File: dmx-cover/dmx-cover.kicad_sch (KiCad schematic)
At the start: 7 parts

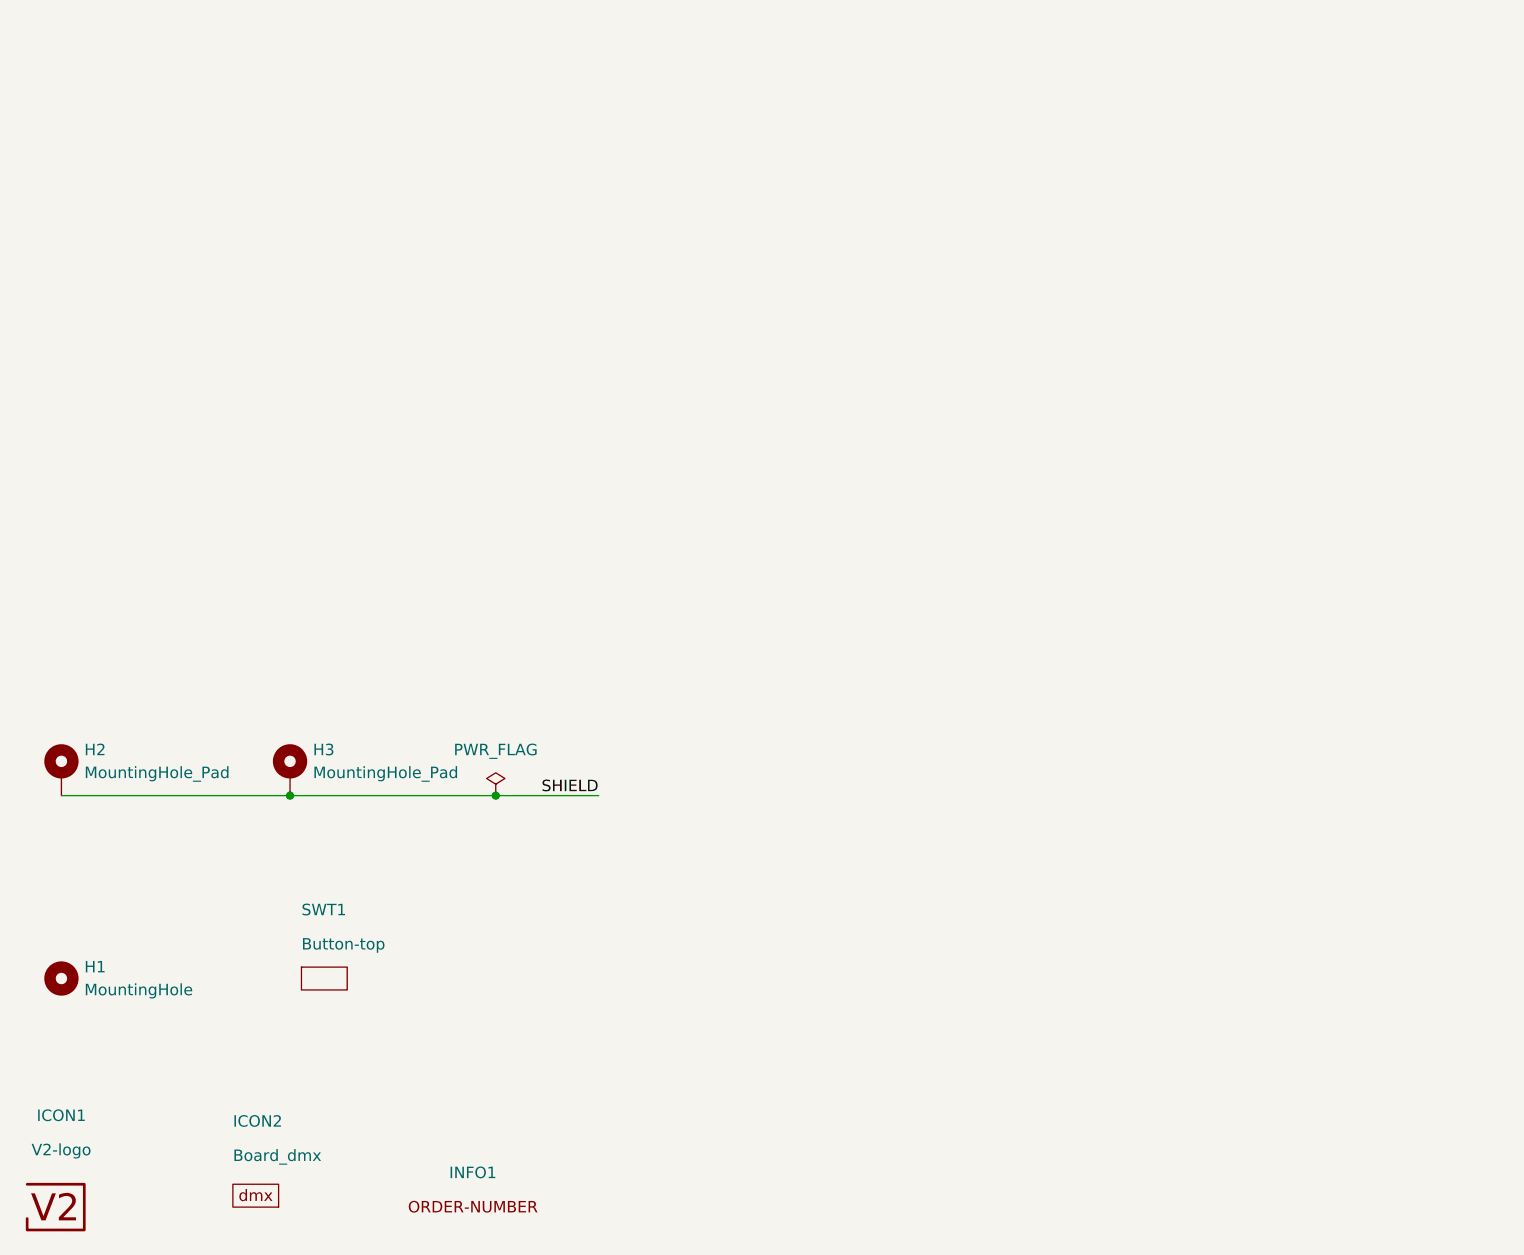
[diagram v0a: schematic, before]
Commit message: Update to KiCad 7.0
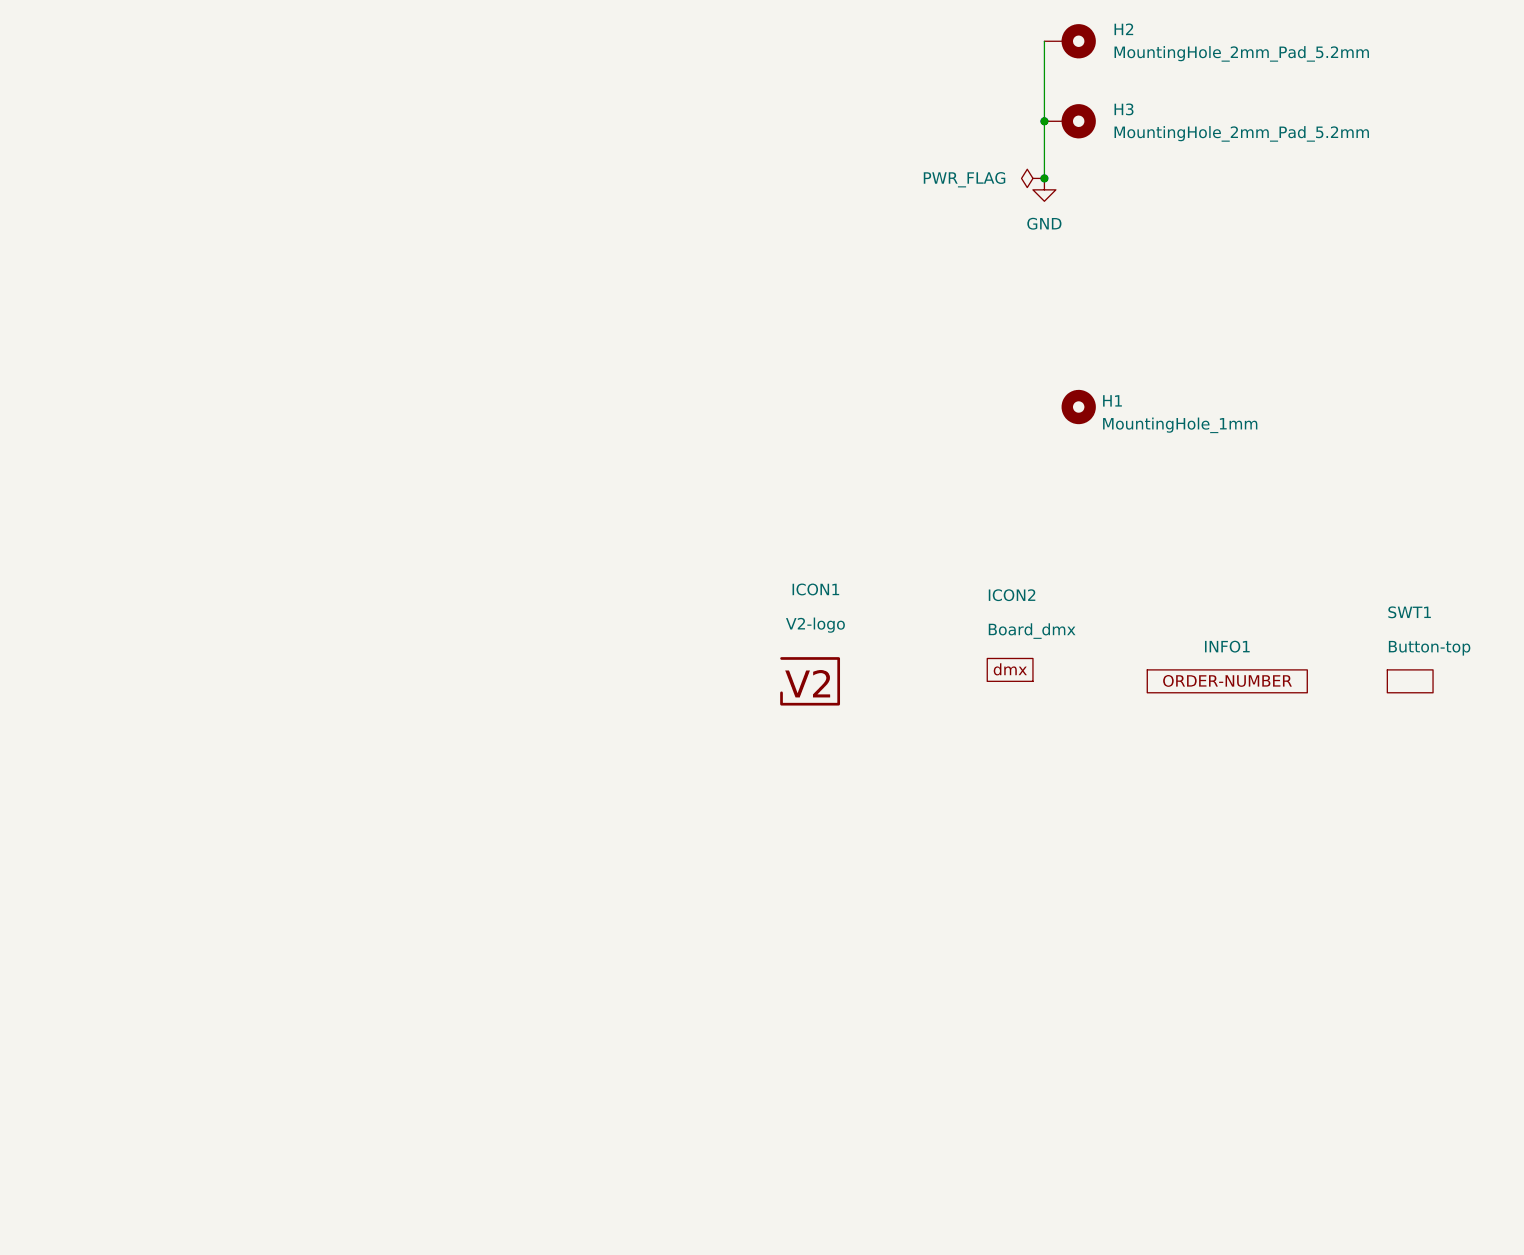
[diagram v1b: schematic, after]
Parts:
- H1: value MountingHole -> MountingHole_1mm; footprint V2_Mechanical:Mounting_Hole_1 -> V2_Mechanical:MountingHole_1mm; symbol Mechanical:MountingHole -> V2_Mechanical:MountingHole_1mm; now left out of the parts list
- H2, H3: value MountingHole_Pad -> MountingHole_2mm_Pad_5.2mm; footprint V2_Mechanical:Mounting_Hole_Pad_2-5.2 -> V2_Mechanical:Mounting_Hole_2mm_Pad_5.2mm; symbol Mechanical:MountingHole_Pad -> V2_Mechanical:MountingHole_2mm_Pad_5.2mm; now left out of the parts list
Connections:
- net SHIELD renamed GND
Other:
- company: (none) -> Versio Dup
- title: (none) -> V2 dmx
- moved on the sheet: H1, H2, H3, ICON1, ICON2, SWT1

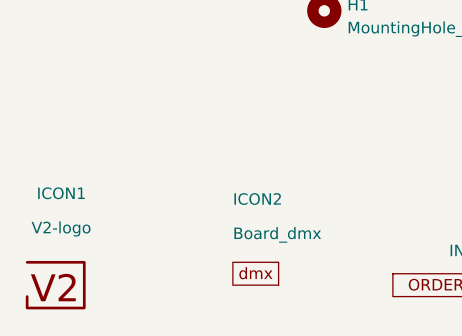
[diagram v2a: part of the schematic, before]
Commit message: Update TRS socket
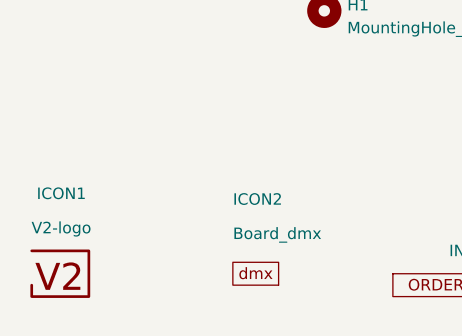
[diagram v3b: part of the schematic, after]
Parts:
- H2, H3: footprint V2_Mechanical:Mounting_Hole_2mm_Pad_5.2mm -> V2_Mechanical:MountingHole_2mm_Pad_5.2mm
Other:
- moved on the sheet: ICON1
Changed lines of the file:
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@@
 			)
 		)
-		(property "Description" ""
+		(property "Description" "Power symbol creates a global label with name \"GND\" , ground"
 			(at 142.24 68.58 0)
 			(effects
@@
 			)
 		)
+		(property "Sim.Enable" "0"
+			(at 138.43 123.19 0)
+			(effects
+				(font
+					(size 1.27 1.27)
+				)
+				(hide yes)
+			)
+		)
 		(instances
 			(project "dmx-cover"
@@
 			)
 		)
+		(property "Sim.Enable" "0"
+			(at 162.56 124.46 0)
+			(effects
+				(font
+					(size 1.27 1.27)
+				)
+				(hide yes)
+			)
+		)
 		(instances
 			(project "dmx-cover"
@@
 			)
 		)
+		(property "Sim.Enable" "0"
+			(at 182.88 124.46 0)
+			(effects
+				(font
+					(size 1.27 1.27)
+				)
+				(hide yes)
+			)
+		)
 		(instances
 			(project "dmx-cover"
@@
 			)
 		)
-		(property "Footprint" "V2_Mechanical:Mounting_Hole_2mm_Pad_5.2mm"
+		(property "Footprint" "V2_Mechanical:MountingHole_2mm_Pad_5.2mm"
 			(at 134.62 53.34 0)
 			(effects
@@
 			)
 		)
-		(property "Description" ""
+		(property "Description" "Mounting Hole with connection"
+			(at 144.78 53.34 0)
+			(effects
+				(font
+					(size 1.27 1.27)
+				)
+				(hide yes)
+			)
+		)
+		(property "Sim.Enable" "0"
 			(at 144.78 53.34 0)
 			(effects
@@
 			)
 		)
-		(property "Description" ""
+		(property "Description" "Special symbol for telling ERC where power comes from"
 			(at 142.24 68.58 0)
 			(effects
@@
 			)
 		)
-		(property "Description" ""
+		(property "Description" "Mounting Hole without connection"
+			(at 146.05 93.98 0)
+			(effects
+				(font
+					(size 1.27 1.27)
+				)
+				(hide yes)
+			)
+		)
+		(property "Sim.Enable" "0"
 			(at 146.05 93.98 0)
 			(effects
@@
 			)
 		)
+		(property "Sim.Enable" "0"
+			(at 116.84 123.19 0)
+			(effects
+				(font
+					(size 1.27 1.27)
+				)
+				(hide yes)
+			)
+		)
 		(instances
 			(project "dmx-cover"
@@
 			)
 		)
-		(property "Footprint" "V2_Mechanical:Mounting_Hole_2mm_Pad_5.2mm"
+		(property "Footprint" "V2_Mechanical:MountingHole_2mm_Pad_5.2mm"
 			(at 134.62 62.23 0)
 			(effects
@@
 			)
 		)
-		(property "Description" ""
+		(property "Description" "Mounting Hole with connection"
 			(at 144.78 62.23 0)
 			(effects
+				(font
+					(size 1.27 1.27)
+				)
+				(hide yes)
+			)
+		)
+		(property "Sim.Enable" "0"
+			(at 144.78 62.23 0)
+			(effects
